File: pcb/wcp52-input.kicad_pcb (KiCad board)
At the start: 4 copper layers, 48.5 x 30.5 mm, 93 parts, among them J1 5V, J3 IN1, J4 IN2, J5 CTRL, J6 PHASEREF, J7 5V, Q1 PMV160UP, Q2 2N7002, Q3 MMBT3906, Q4 2N7002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

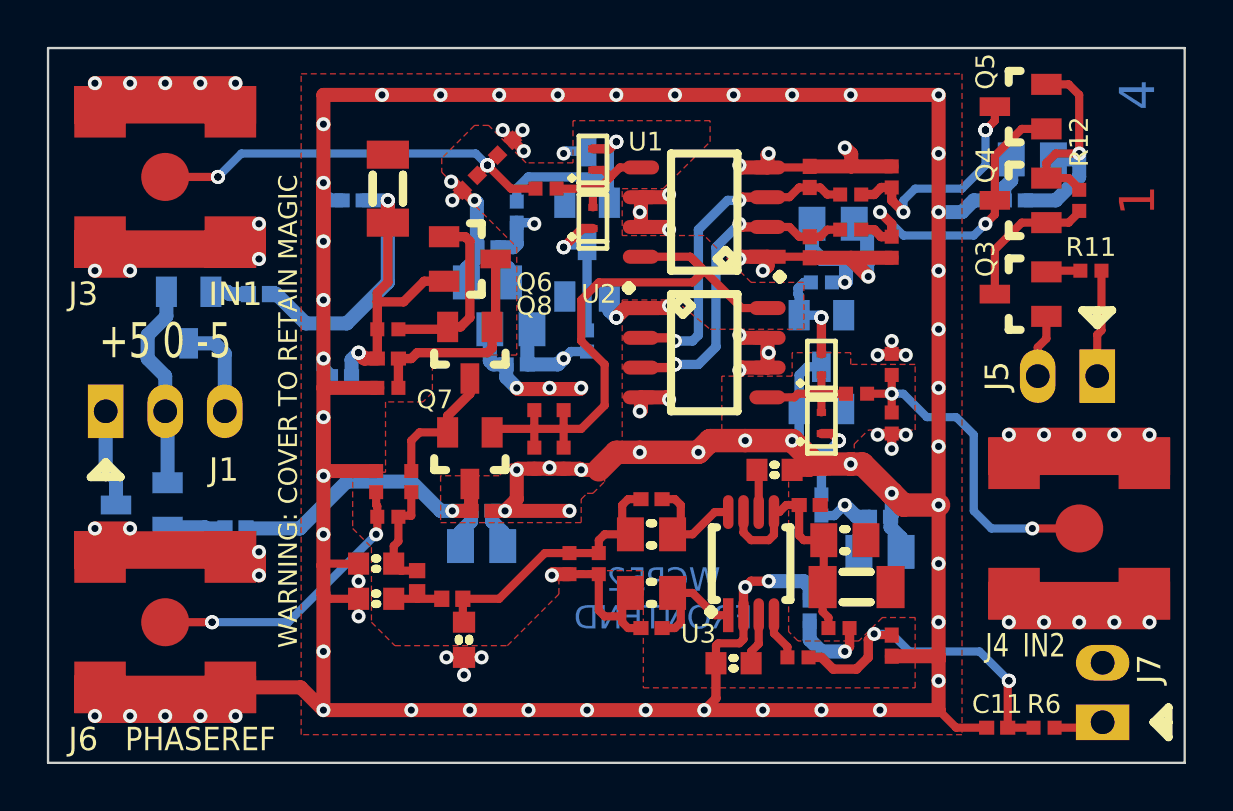
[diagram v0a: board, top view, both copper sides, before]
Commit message: Rearranged to fit visible refdes
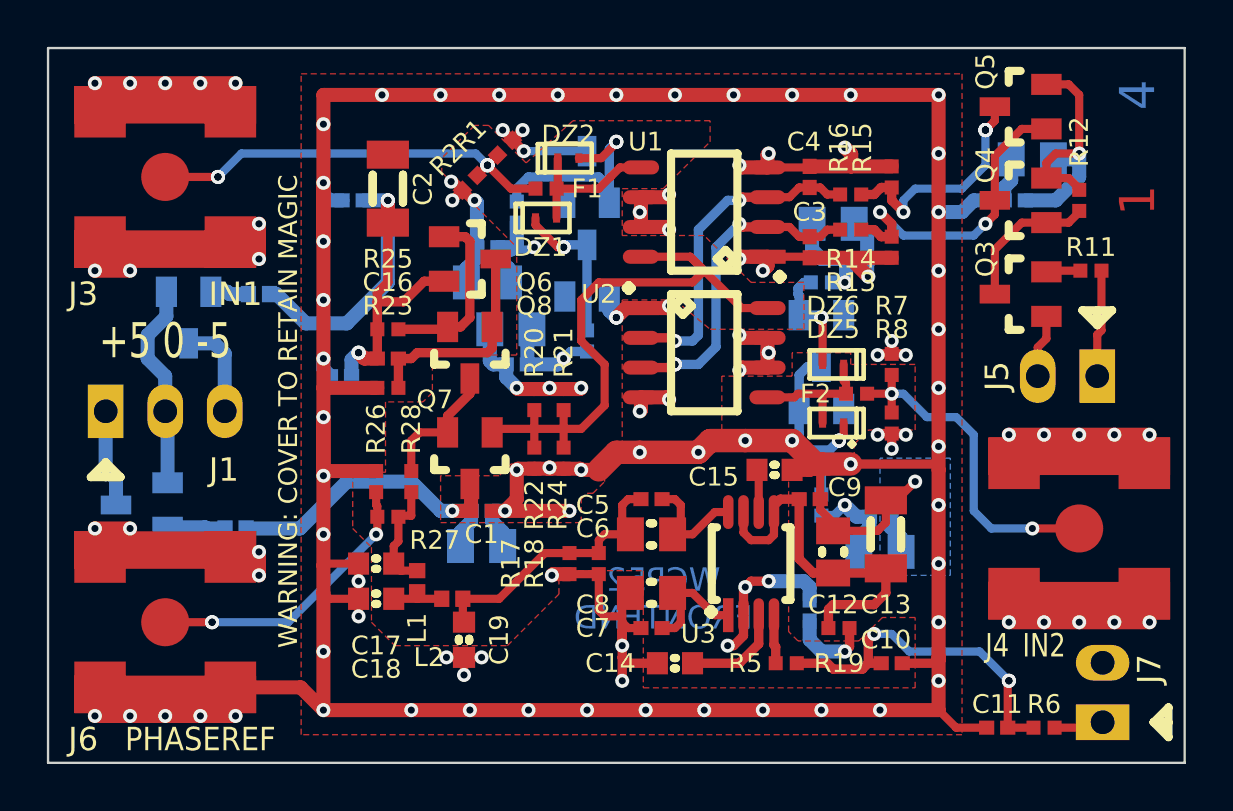
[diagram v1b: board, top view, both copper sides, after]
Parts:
- moved C13 2.57 mm to (122.8, 80.2), turned to 90 degrees
- moved C14 2.50 mm to (113.8, 85.8)
- moved DZ1 2.00 mm to (108.2, 66.8), turned to 0 degrees
- moved DZ2 1.05 mm to (109.2, 64.2), turned to 0 degrees
- moved C10 0.75 mm to (123.0, 85.8), turned to 0 degrees
- moved C12 0.71 mm to (120.5, 81.0), turned to 270 degrees
- moved R5 0.56 mm to (118.5, 85.8)
- moved DZ5 0.50 mm to (120.5, 75.5), turned to 180 degrees
- moved DZ6 0.50 mm to (120.5, 73.0), turned to 180 degrees
- moved C9 0.25 mm to (119.5, 78.8)
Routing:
- net GND: track 321.7 -> 330.8 mm, vias 119 -> 121
- net /Detector/4V6_FILTERED: track 10.9 -> 16.0 mm
- net Net-(C14-Pad1): track 2.18 -> 4.39 mm
- net /Switching/IN2: track 5.01 -> 5.93 mm
- net /Switching/IN1: track 5.65 -> 6.55 mm
- net Net-(DZ2-Pad2): track 9.39 -> 10.2 mm
- net -5: track 44.4 -> 44.9 mm
- added copper zone on B.Cu, net GND

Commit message: Switched to PTH SMA connectors
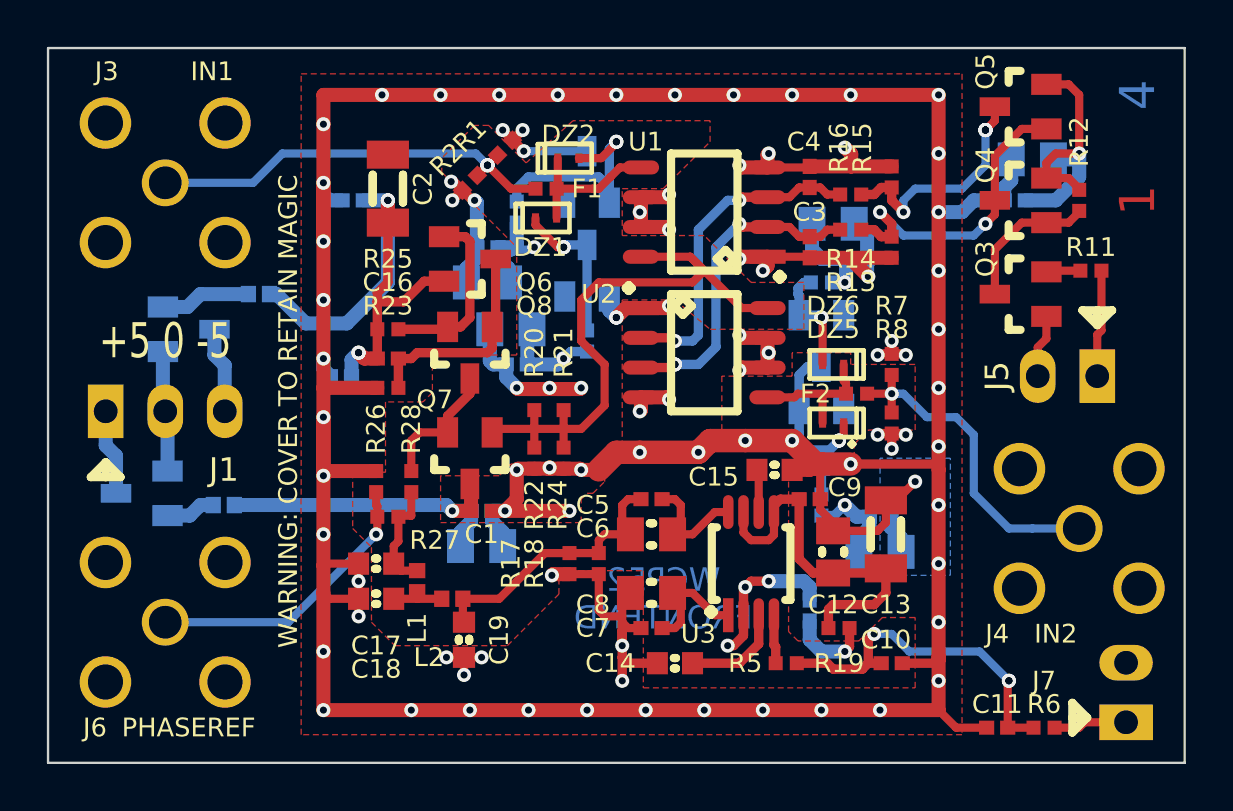
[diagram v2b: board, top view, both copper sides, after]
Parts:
- J3, J4, J6: footprint conn:CONN-2_CONSMA001-SMD-G -> conn:CONN-2_CONSMA001
- L1, L2: value 27n 2% -> 39n 2%
- moved E1 1.12 mm to (94.5, 79.0)
- moved J7 1.00 mm to (133.0, 87.0)
- moved Q1 0.50 mm to (91.0, 78.5)
- moved Q2 0.50 mm to (93.0, 71.5), turned to 0 degrees
- moved J3 0.25 mm to (92.0, 65.2), turned to 0 degrees
- turned J4 to 0 degrees
- turned J6 to 0 degrees
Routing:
- net GND: track 330.8 -> 253.3 mm, vias 121 -> 93
- net Net-(E2-Pad1): track 1.64 -> 3.88 mm
- net Net-(J7-Pad1): track 2.15 -> 3.15 mm
- net +5: track 26.7 -> 26.0 mm
- net Net-(J1-Pad3): track 4.18 -> 3.68 mm
- net Net-(J1-Pad1): track 4.18 -> 3.68 mm
- net /Protection/IN2: track 14.9 -> 14.5 mm, vias 2 -> 1
- net /Protection/IN1: track 18.1 -> 18.2 mm, vias 5 -> 3
- net /Buffer_Filter/PHASEREF: vias 3 -> 1
